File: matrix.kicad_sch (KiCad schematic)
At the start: 174 parts

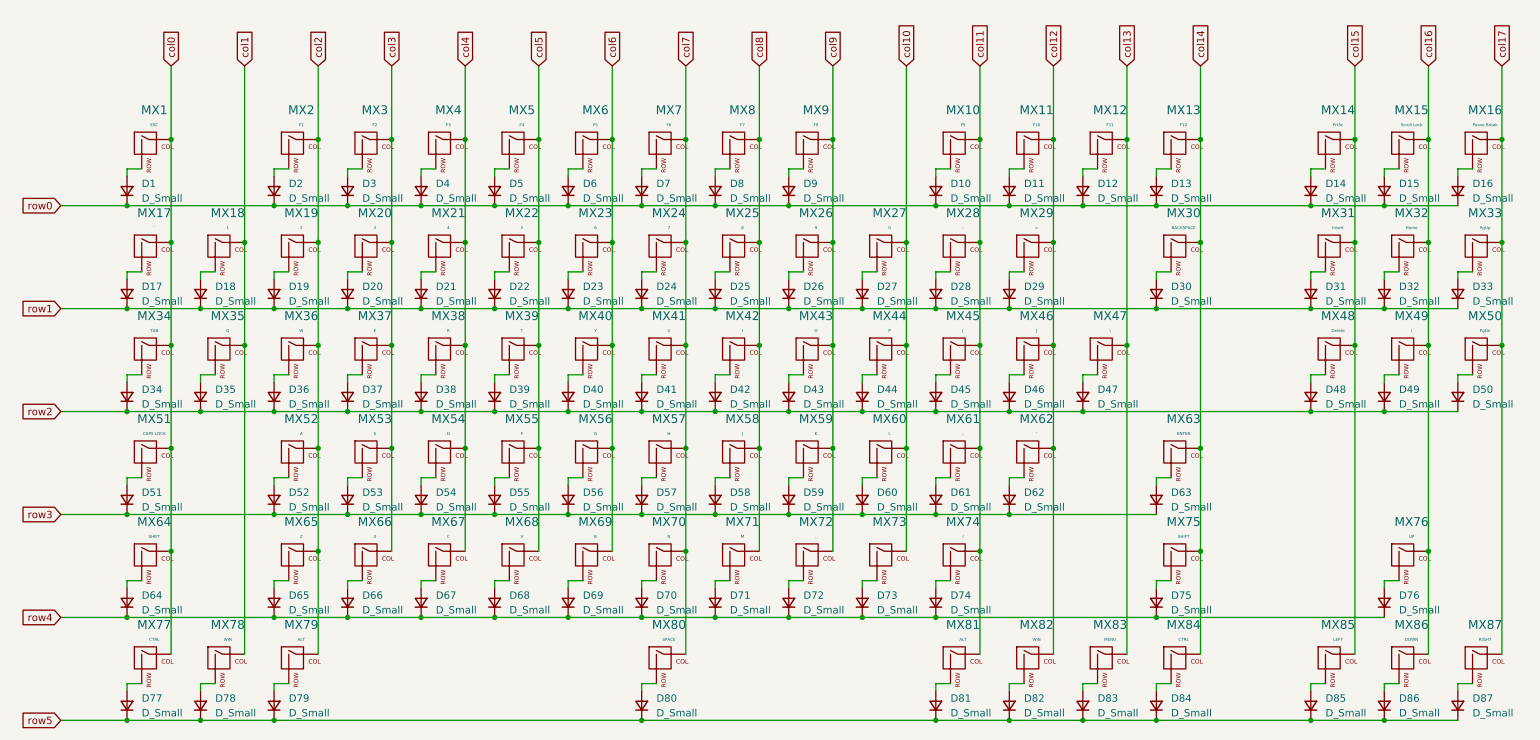
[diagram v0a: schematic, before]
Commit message: Assigned footprints to components
Also edited layout slightly (7u spacebar and removal of PrtSc, ScLk, Pause)
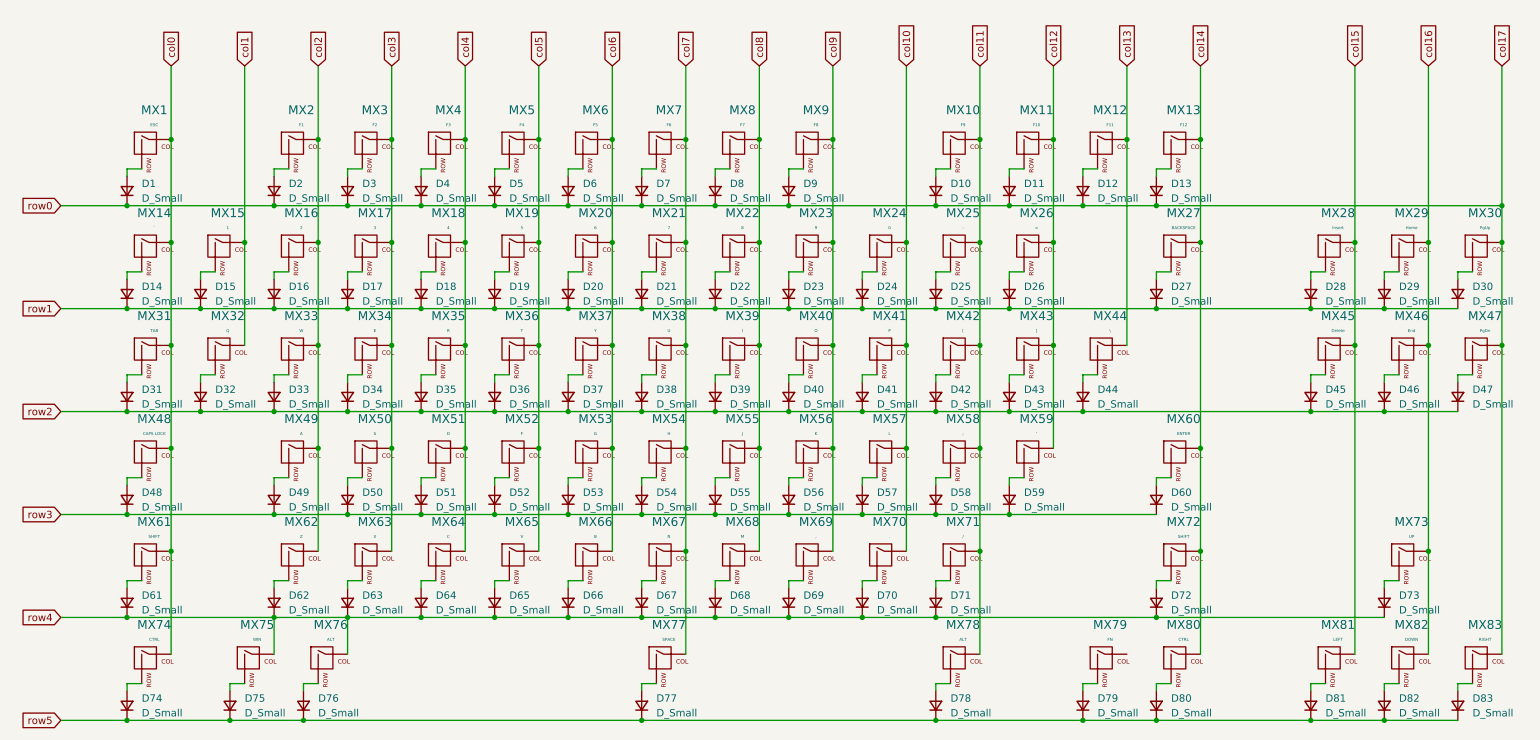
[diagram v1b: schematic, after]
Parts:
- removed D14, D15, D16, D81: D_Small, symbol Device:D_Small
- removed MX14: PrtSc, symbol MX_Alps_Hybrid:MX-NoLED
- removed MX15: Scroll Lock, symbol MX_Alps_Hybrid:MX-NoLED
- removed MX16: Pause Break, symbol MX_Alps_Hybrid:MX-NoLED
- removed MX81: ALT, symbol MX_Alps_Hybrid:MX-NoLED
- D1, D10, D11, D12, D13, D2, D3, D4, D5, D6, D7, D8, D9: footprint (none) -> Diode_SMD:D_SOD-123
- D14: renamed from D17; footprint (none) -> Diode_SMD:D_SOD-123
- D15: renamed from D18; footprint (none) -> Diode_SMD:D_SOD-123
- D16: renamed from D19; footprint (none) -> Diode_SMD:D_SOD-123
- D17: renamed from D20; footprint (none) -> Diode_SMD:D_SOD-123
- D18: renamed from D21; footprint (none) -> Diode_SMD:D_SOD-123
- D19: renamed from D22; footprint (none) -> Diode_SMD:D_SOD-123
- D20: renamed from D23; footprint (none) -> Diode_SMD:D_SOD-123
- D21: renamed from D24; footprint (none) -> Diode_SMD:D_SOD-123
- D22: renamed from D25; footprint (none) -> Diode_SMD:D_SOD-123
- D23: renamed from D26; footprint (none) -> Diode_SMD:D_SOD-123
- D24: renamed from D27; footprint (none) -> Diode_SMD:D_SOD-123
- D25: renamed from D28; footprint (none) -> Diode_SMD:D_SOD-123
- D26: renamed from D29; footprint (none) -> Diode_SMD:D_SOD-123
- D27: renamed from D30; footprint (none) -> Diode_SMD:D_SOD-123
- D28: renamed from D31; footprint (none) -> Diode_SMD:D_SOD-123
- D29: renamed from D32; footprint (none) -> Diode_SMD:D_SOD-123
- D30: renamed from D33; footprint (none) -> Diode_SMD:D_SOD-123
- D31: renamed from D34; footprint (none) -> Diode_SMD:D_SOD-123
- D32: renamed from D35; footprint (none) -> Diode_SMD:D_SOD-123
- D33: renamed from D36; footprint (none) -> Diode_SMD:D_SOD-123
- D34: renamed from D37; footprint (none) -> Diode_SMD:D_SOD-123
- D35: renamed from D38; footprint (none) -> Diode_SMD:D_SOD-123
- D36: renamed from D39; footprint (none) -> Diode_SMD:D_SOD-123
- D37: renamed from D40; footprint (none) -> Diode_SMD:D_SOD-123
- D38: renamed from D41; footprint (none) -> Diode_SMD:D_SOD-123
- D39: renamed from D42; footprint (none) -> Diode_SMD:D_SOD-123
- D40: renamed from D43; footprint (none) -> Diode_SMD:D_SOD-123
- D41: renamed from D44; footprint (none) -> Diode_SMD:D_SOD-123
- D42: renamed from D45; footprint (none) -> Diode_SMD:D_SOD-123
- D43: renamed from D46; footprint (none) -> Diode_SMD:D_SOD-123
- D44: renamed from D47; footprint (none) -> Diode_SMD:D_SOD-123
- D45: renamed from D48; footprint (none) -> Diode_SMD:D_SOD-123
- D46: renamed from D49; footprint (none) -> Diode_SMD:D_SOD-123
- D47: renamed from D50; footprint (none) -> Diode_SMD:D_SOD-123
- D48: renamed from D51; footprint (none) -> Diode_SMD:D_SOD-123
- D49: renamed from D52; footprint (none) -> Diode_SMD:D_SOD-123
- D50: renamed from D53; footprint (none) -> Diode_SMD:D_SOD-123
- D51: renamed from D54; footprint (none) -> Diode_SMD:D_SOD-123
- D52: renamed from D55; footprint (none) -> Diode_SMD:D_SOD-123
- D53: renamed from D56; footprint (none) -> Diode_SMD:D_SOD-123
- D54: renamed from D57; footprint (none) -> Diode_SMD:D_SOD-123
- D55: renamed from D58; footprint (none) -> Diode_SMD:D_SOD-123
- D56: renamed from D59; footprint (none) -> Diode_SMD:D_SOD-123
- D57: renamed from D60; footprint (none) -> Diode_SMD:D_SOD-123
- D58: renamed from D61; footprint (none) -> Diode_SMD:D_SOD-123
- D59: renamed from D62; footprint (none) -> Diode_SMD:D_SOD-123
- D60: renamed from D63; footprint (none) -> Diode_SMD:D_SOD-123
- D61: renamed from D64; footprint (none) -> Diode_SMD:D_SOD-123
- D62: renamed from D65; footprint (none) -> Diode_SMD:D_SOD-123
- D63: renamed from D66; footprint (none) -> Diode_SMD:D_SOD-123
- D64: renamed from D67; footprint (none) -> Diode_SMD:D_SOD-123
- D65: renamed from D68; footprint (none) -> Diode_SMD:D_SOD-123
- D66: renamed from D69; footprint (none) -> Diode_SMD:D_SOD-123
- D67: renamed from D70; footprint (none) -> Diode_SMD:D_SOD-123
- D68: renamed from D71; footprint (none) -> Diode_SMD:D_SOD-123
- D69: renamed from D72; footprint (none) -> Diode_SMD:D_SOD-123
- D70: renamed from D73; footprint (none) -> Diode_SMD:D_SOD-123
- D71: renamed from D74; footprint (none) -> Diode_SMD:D_SOD-123
- D72: renamed from D75; footprint (none) -> Diode_SMD:D_SOD-123
- D73: renamed from D76; footprint (none) -> Diode_SMD:D_SOD-123
- D74: renamed from D77; footprint (none) -> Diode_SMD:D_SOD-123
- D75: renamed from D78; footprint (none) -> Diode_SMD:D_SOD-123
- D76: renamed from D79; footprint (none) -> Diode_SMD:D_SOD-123
- D77: renamed from D80; footprint (none) -> Diode_SMD:D_SOD-123
- D78: renamed from D82; footprint (none) -> Diode_SMD:D_SOD-123
- D79: renamed from D83; footprint (none) -> Diode_SMD:D_SOD-123
- D80: renamed from D84; footprint (none) -> Diode_SMD:D_SOD-123
- D81: renamed from D85; footprint (none) -> Diode_SMD:D_SOD-123
- D82: renamed from D86; footprint (none) -> Diode_SMD:D_SOD-123
- D83: renamed from D87; footprint (none) -> Diode_SMD:D_SOD-123
- MX1, MX10, MX11, MX12, MX13, MX2, MX3, MX4, MX5, MX6, MX7, MX8, MX9: footprint (none) -> MX_Hotswap:MX-Hotswap-1U
- MX14: renamed from MX17; footprint (none) -> MX_Hotswap:MX-Hotswap-1U
- MX15: renamed from MX18; footprint (none) -> MX_Hotswap:MX-Hotswap-1U
- MX16: renamed from MX19; footprint (none) -> MX_Hotswap:MX-Hotswap-1U
- MX17: renamed from MX20; footprint (none) -> MX_Hotswap:MX-Hotswap-1U
- MX18: renamed from MX21; footprint (none) -> MX_Hotswap:MX-Hotswap-1U
- MX19: renamed from MX22; footprint (none) -> MX_Hotswap:MX-Hotswap-1U
- MX20: renamed from MX23; footprint (none) -> MX_Hotswap:MX-Hotswap-1U
- MX21: renamed from MX24; footprint (none) -> MX_Hotswap:MX-Hotswap-1U
- MX22: renamed from MX25; footprint (none) -> MX_Hotswap:MX-Hotswap-1U
- MX23: renamed from MX26; footprint (none) -> MX_Hotswap:MX-Hotswap-1U
- MX24: renamed from MX27; footprint (none) -> MX_Hotswap:MX-Hotswap-1U
- MX25: renamed from MX28; footprint (none) -> MX_Hotswap:MX-Hotswap-1U
- MX26: renamed from MX29; footprint (none) -> MX_Hotswap:MX-Hotswap-1U
- MX27: renamed from MX30; footprint (none) -> MX_Hotswap:MX-Hotswap-2U
- MX28: renamed from MX31; footprint (none) -> MX_Hotswap:MX-Hotswap-1U
- MX29: renamed from MX32; footprint (none) -> MX_Hotswap:MX-Hotswap-1U
- MX30: renamed from MX33; footprint (none) -> MX_Hotswap:MX-Hotswap-1U
- MX31: renamed from MX34; footprint (none) -> MX_Hotswap:MX-Hotswap-1.5U
- MX32: renamed from MX35; footprint (none) -> MX_Hotswap:MX-Hotswap-1U
- MX33: renamed from MX36; footprint (none) -> MX_Hotswap:MX-Hotswap-1U
- MX34: renamed from MX37; footprint (none) -> MX_Hotswap:MX-Hotswap-1U
- MX35: renamed from MX38; footprint (none) -> MX_Hotswap:MX-Hotswap-1U
- MX36: renamed from MX39; footprint (none) -> MX_Hotswap:MX-Hotswap-1U
- MX37: renamed from MX40; footprint (none) -> MX_Hotswap:MX-Hotswap-1U
- MX38: renamed from MX41; footprint (none) -> MX_Hotswap:MX-Hotswap-1U
- MX39: renamed from MX42; footprint (none) -> MX_Hotswap:MX-Hotswap-1U
- MX40: renamed from MX43; footprint (none) -> MX_Hotswap:MX-Hotswap-1U
- MX41: renamed from MX44; footprint (none) -> MX_Hotswap:MX-Hotswap-1U
- MX42: renamed from MX45; footprint (none) -> MX_Hotswap:MX-Hotswap-1U
- MX43: renamed from MX46; footprint (none) -> MX_Hotswap:MX-Hotswap-1U
- MX44: renamed from MX47; footprint (none) -> MX_Hotswap:MX-Hotswap-1.5U
- MX45: renamed from MX48; footprint (none) -> MX_Hotswap:MX-Hotswap-1U
- MX46: renamed from MX49; value \ -> End; footprint (none) -> MX_Hotswap:MX-Hotswap-1U
- MX47: renamed from MX50; footprint (none) -> MX_Hotswap:MX-Hotswap-1U
- MX48: renamed from MX51; footprint (none) -> MX_Hotswap:MX-Hotswap-1.75U
- MX49: renamed from MX52; footprint (none) -> MX_Hotswap:MX-Hotswap-1U
- MX50: renamed from MX53; footprint (none) -> MX_Hotswap:MX-Hotswap-1U
- MX51: renamed from MX54; footprint (none) -> MX_Hotswap:MX-Hotswap-1U
- MX52: renamed from MX55; footprint (none) -> MX_Hotswap:MX-Hotswap-1U
- MX53: renamed from MX56; footprint (none) -> MX_Hotswap:MX-Hotswap-1U
- MX54: renamed from MX57; footprint (none) -> MX_Hotswap:MX-Hotswap-1U
- MX55: renamed from MX58; footprint (none) -> MX_Hotswap:MX-Hotswap-1U
- MX56: renamed from MX59; footprint (none) -> MX_Hotswap:MX-Hotswap-1U
- MX57: renamed from MX60; footprint (none) -> MX_Hotswap:MX-Hotswap-1U
- MX58: renamed from MX61; footprint (none) -> MX_Hotswap:MX-Hotswap-1U
- MX59: renamed from MX62; footprint (none) -> MX_Hotswap:MX-Hotswap-1U
- MX60: renamed from MX63; footprint (none) -> MX_Hotswap:MX-Hotswap-2.25U
- MX61: renamed from MX64; footprint (none) -> MX_Hotswap:MX-Hotswap-2.25U
- MX62: renamed from MX65; footprint (none) -> MX_Hotswap:MX-Hotswap-1U
- MX63: renamed from MX66; footprint (none) -> MX_Hotswap:MX-Hotswap-1U
- MX64: renamed from MX67; footprint (none) -> MX_Hotswap:MX-Hotswap-1U
- MX65: renamed from MX68; footprint (none) -> MX_Hotswap:MX-Hotswap-1U
- MX66: renamed from MX69; footprint (none) -> MX_Hotswap:MX-Hotswap-1U
- MX67: renamed from MX70; footprint (none) -> MX_Hotswap:MX-Hotswap-1U
- MX68: renamed from MX71; footprint (none) -> MX_Hotswap:MX-Hotswap-1U
- MX69: renamed from MX72; footprint (none) -> MX_Hotswap:MX-Hotswap-1U
- MX70: renamed from MX73; footprint (none) -> MX_Hotswap:MX-Hotswap-1U
- MX71: renamed from MX74; footprint (none) -> MX_Hotswap:MX-Hotswap-1U
- MX72: renamed from MX75; footprint (none) -> MX_Hotswap:MX-Hotswap-2.75U
- MX73: renamed from MX76; footprint (none) -> MX_Hotswap:MX-Hotswap-1U
- MX74: renamed from MX77; footprint (none) -> MX_Hotswap:MX-Hotswap-1.5U
- MX75: renamed from MX78; footprint (none) -> MX_Hotswap:MX-Hotswap-1U
- MX76: renamed from MX79; footprint (none) -> MX_Hotswap:MX-Hotswap-1.5U
- MX77: renamed from MX80; footprint (none) -> MX_Hotswap:MX-Hotswap-7U
- MX78: renamed from MX82; value WIN -> ALT; footprint (none) -> MX_Hotswap:MX-Hotswap-1.5U
- MX79: renamed from MX83; value MENU -> FN; footprint (none) -> MX_Hotswap:MX-Hotswap-1U
- MX80: renamed from MX84; footprint (none) -> MX_Hotswap:MX-Hotswap-1.5U
- MX81: renamed from MX85; footprint (none) -> MX_Hotswap:MX-Hotswap-1U
- MX82: renamed from MX86; footprint (none) -> MX_Hotswap:MX-Hotswap-1U
- MX83: renamed from MX87; footprint (none) -> MX_Hotswap:MX-Hotswap-1U
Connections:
- net row0 is gone; now on net col17: D1.1 (K), D10.1 (K), D11.1 (K), D12.1 (K), D13.1 (K), D2.1 (K), D3.1 (K), D4.1 (K), D5.1 (K), D6.1 (K), D7.1 (K), D8.1 (K), D9.1 (K)
- net col1: no longer MX75.1 (COL)
- net col11: now also MX78.1 (COL)
- net col12: no longer MX78.1 (COL)
- net col13: no longer MX79.1 (COL)
- net col2: no longer MX76.1 (COL)
- net row4: now also MX75.1 (COL), MX76.1 (COL)
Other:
- moved on the sheet: D75, D76, D78, MX75, MX76, MX78

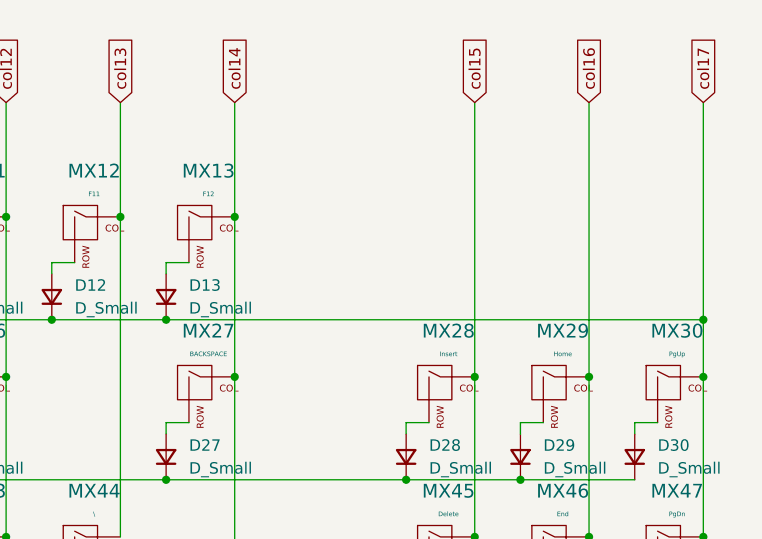
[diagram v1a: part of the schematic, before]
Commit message: Wired MCU loop on PCB
All components of MCU loop wired together, keyswitch matrix remaining
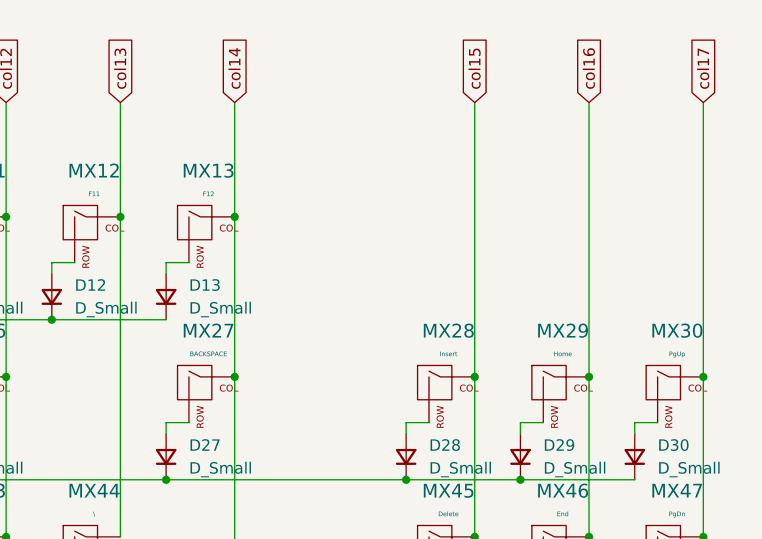
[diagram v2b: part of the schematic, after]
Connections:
- net col17: no longer D1.1 (K), D10.1 (K), D11.1 (K), D12.1 (K), D13.1 (K), D2.1 (K), D3.1 (K), D4.1 (K), D5.1 (K), D6.1 (K), D7.1 (K), D8.1 (K), D9.1 (K)
- new net row0: D1.1 (K), D10.1 (K), D11.1 (K), D12.1 (K), D13.1 (K), D2.1 (K), D3.1 (K), D4.1 (K), D5.1 (K), D6.1 (K), D7.1 (K), D8.1 (K), D9.1 (K)
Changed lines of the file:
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@@
-	)
-	(junction
-		(at 275.59 62.23)
-		(diameter 0)
-		(color 0 0 0 0)
 	)
 	(junction
@@
 	)
 	(junction
-		(at 215.9 62.23)
-		(diameter 0)
-		(color 0 0 0 0)
-	)
-	(junction
 		(at 185.42 50.8)
 		(diameter 0)
@@
 	(wire
 		(pts
-			(xy 215.9 62.23) (xy 275.59 62.23)
-		)
-		(stroke
-			(width 0)
-			(type default)
-		)
-	)
-	(wire
-		(pts
 			(xy 172.72 68.58) (xy 172.72 86.36)
 		)
@@
 	(wire
 		(pts
-			(xy 275.59 38.1) (xy 275.59 62.23)
-		)
-		(stroke
-			(width 0)
-			(type default)
-		)
-	)
-	(wire
-		(pts
 			(xy 88.9 57.15) (xy 88.9 55.88)
 		)
@@
 	(wire
 		(pts
-			(xy 275.59 62.23) (xy 275.59 68.58)
-		)
-		(stroke
+			(xy 275.59 38.1) (xy 275.59 68.58)
+		)
+		(stroke
